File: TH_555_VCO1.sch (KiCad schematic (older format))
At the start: 73 parts, among them J601 CV1, J602 FM_lin, J603 Sync, J604 PWM, J605 Ramp, J606 Tri, J607 Sine, J608 555_Pulse, P601 Doepfer_Power_16pin, Q601 MMBT2222A, U601 TLC555, U602 TL074, U603 TL074

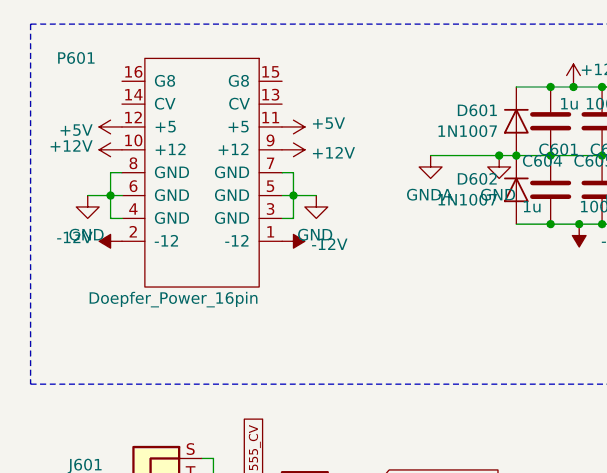
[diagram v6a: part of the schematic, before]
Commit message: 16p -> 10p on 555 VCO
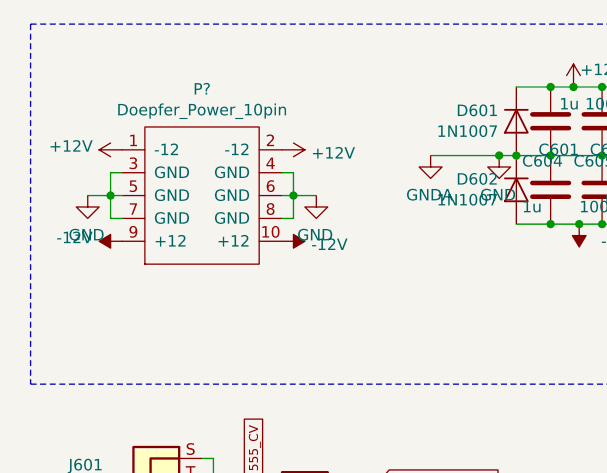
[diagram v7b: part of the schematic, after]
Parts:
- removed P601: Doepfer_Power_16pin, Connectors_IDC:IDC-Header_2x08_Pitch2.54mm_Straight, symbol Eurorack:Doepfer_Power_16pin
- added P?: Doepfer_Power_10pin, Connectors_IDC:IDC-Header_2x05_Pitch2.54mm_Straight, symbol Eurorack:Doepfer_Power_10pin
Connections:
- net +12V: now also P?.1 (-12), P?.2 (-12)
- net -12V: now also P?.10 (+12), P?.9 (+12)
- net GND: now also P?.3 (GND), P?.4 (GND), P?.5 (GND), P?.6 (GND), P?.7 (GND), P?.8 (GND)
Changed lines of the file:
@@
 $EndDescr
-$Comp
-L Eurorack:Doepfer_Power_16pin P?
-U 1 1 5DD8FB20
-P 1275 1175
-AR Path="/5DD8FB20" Ref="P?"  Part="1"
-AR Path="/5CE53731/5DD8FB20" Ref="P?"  Part="1"
-AR Path="/5DD87D87/5DD8FB20" Ref="P601"  Part="1"
-F 0 "P601" H 1825 675 50  0000 C CNN
-F 1 "Doepfer_Power_16pin" H 1400 1725 50  0000 C CNN
-F 2 "Connectors_IDC:IDC-Header_2x08_Pitch2.54mm_Straight" H 1275 1175 50  0001 C CNN
-F 3 "" H 1275 1175 50  0001 C CNN
-	1    1275 1175
-	-1   0    0    1
-$EndComp
-$Comp
-L Envelope-cache-2018-08-04-13-00-04:+5V #PWR?
-U 1 1 5DD8FB26
-P 1625 975
-AR Path="/5DD8FB26" Ref="#PWR?"  Part="1"
-AR Path="/5CE53731/5DD8FB26" Ref="#PWR?"  Part="1"
-AR Path="/5DD87D87/5DD8FB26" Ref="#PWR0606"  Part="1"
-F 0 "#PWR0606" H 1625 825 50  0001 C CNN
-F 1 "+5V" V 1640 1103 50  0000 L CNN
-F 2 "" H 1625 975 50  0001 C CNN
-F 3 "" H 1625 975 50  0001 C CNN
-	1    1625 975
-	0    1    -1   0
-$EndComp
-$Comp
-L Envelope-cache-2018-08-04-13-00-04:+5V #PWR?
-U 1 1 5DD8FB2C
-P 925 975
-AR Path="/5DD8FB2C" Ref="#PWR?"  Part="1"
-AR Path="/5CE53731/5DD8FB2C" Ref="#PWR?"  Part="1"
-AR Path="/5DD87D87/5DD8FB2C" Ref="#PWR0605"  Part="1"
-F 0 "#PWR0605" H 925 825 50  0001 C CNN
-F 1 "+5V" V 940 1103 50  0000 L CNN
-F 2 "" H 925 975 50  0001 C CNN
-F 3 "" H 925 975 50  0001 C CNN
-	1    925  975
-	0    -1   1    0
-$EndComp
 $Comp
 L Envelope-cache-2018-08-04-13-00-04:+12V #PWR?
@@
 	1    1625 1075
 	0    1    1    0
-$EndComp
-$Comp
-L Envelope-cache-2018-08-04-13-00-04:+12V #PWR?
-U 1 1 5DD8FB38
-P 925 1075
-AR Path="/5DD8FB38" Ref="#PWR?"  Part="1"
-AR Path="/5CE53731/5DD8FB38" Ref="#PWR?"  Part="1"
-AR Path="/5DD87D87/5DD8FB38" Ref="#PWR0607"  Part="1"
-F 0 "#PWR0607" H 925 925 50  0001 C CNN
-F 1 "+12V" V 940 1203 50  0000 L CNN
-F 2 "" H 925 1075 50  0001 C CNN
-F 3 "" H 925 1075 50  0001 C CNN
-	1    925  1075
-	0    -1   -1   0
 $EndComp
 $Comp
@@
 Text GLabel 10750 1225 2    39   Input ~ 0
 555_In
-Wire Notes Line
-	525  525  525  2100
 Wire Notes Line
 	525  2100 11150 2100
@@
 Text GLabel 10525 5525 2    39   Input ~ 0
 555_Pulse
+$Comp
+L Eurorack:Doepfer_Power_10pin P?
+U 1 1 5E362A15
+P 1275 1375
+F 0 "P?" H 1275 1940 50  0000 C CNN
+F 1 "Doepfer_Power_10pin" H 1275 1849 50  0000 C CNN
+F 2 "Connectors_IDC:IDC-Header_2x05_Pitch2.54mm_Straight" H 1275 1375 50  0001 C CNN
+F 3 "" H 1275 1375 50  0001 C CNN
+	1    1275 1375
+	1    0    0    -1
+$EndComp
+Wire Notes Line
+	525  525  525  2100
+$Comp
+L Envelope-cache-2018-08-04-13-00-04:+12V #PWR?
+U 1 1 5DD8FB38
+P 925 1075
+AR Path="/5DD8FB38" Ref="#PWR?"  Part="1"
+AR Path="/5CE53731/5DD8FB38" Ref="#PWR?"  Part="1"
+AR Path="/5DD87D87/5DD8FB38" Ref="#PWR0607"  Part="1"
+F 0 "#PWR0607" H 925 925 50  0001 C CNN
+F 1 "+12V" V 940 1203 50  0000 L CNN
+F 2 "" H 925 1075 50  0001 C CNN
+F 3 "" H 925 1075 50  0001 C CNN
+	1    925  1075
+	0    -1   -1   0
+$EndComp
 $EndSCHEMATC

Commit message: 555 PCB
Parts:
- D611: footprint (none) -> LED_THT:LED_D3.0mm
- Q601: footprint SOT23 -> Package_TO_SOT_SMD:SOT-23
- RV602: footprint (none) -> Potentiometer_THT:Potentiometer_Piher_PT-6-V_Vertical
- gave numbers to parts that had none: 1
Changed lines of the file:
@@
 F 0 "Q601" H 6944 1071 50  0000 L CNN
 F 1 "MMBT2222A" H 6400 875 50  0000 L CNN
-F 2 "SOT23" H 6800 1025 50  0001 L BNN
+F 2 "Package_TO_SOT_SMD:SOT-23" H 6800 1025 50  0001 L BNN
 F 3 "" H 6800 1025 50  0001 L BNN
 F 4 "None" H 6800 1025 50  0001 L BNN "Field4"
@@
 F 0 "RV602" V 2643 6775 50  0000 C CNN
 F 1 "5k" V 2734 6775 50  0000 C CNN
-F 2 "" H 2850 6775 50  0001 C CNN
+F 2 "Potentiometer_THT:Potentiometer_Piher_PT-6-V_Vertical" H 2850 6775 50  0001 C CNN
 F 3 "~" H 2850 6775 50  0001 C CNN
 	1    2850 6775
@@
 F 0 "D611" V 3039 6958 50  0000 R CNN
 F 1 "Vactrol" V 2948 6958 50  0000 R CNN
-F 2 "" H 3000 7075 50  0001 C CNN
+F 2 "LED_THT:LED_D3.0mm" H 3000 7075 50  0001 C CNN
 F 3 "~" H 3000 7075 50  0001 C CNN
 	1    3000 7075
@@
 555_Pulse
 $Comp
-L Eurorack:Doepfer_Power_10pin P?
+L Eurorack:Doepfer_Power_10pin P601
 U 1 1 5E362A15
 P 1275 1375
-F 0 "P?" H 1275 1940 50  0000 C CNN
+F 0 "P601" H 1275 1940 50  0000 C CNN
 F 1 "Doepfer_Power_10pin" H 1275 1849 50  0000 C CNN
 F 2 "Connectors_IDC:IDC-Header_2x05_Pitch2.54mm_Straight" H 1275 1375 50  0001 C CNN
